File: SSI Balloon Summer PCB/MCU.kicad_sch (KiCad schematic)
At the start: 19 parts, among them J5 Conn_01x05, J9 Camera, SW2 SW_SPST, SW3 SW_SPST, U7 STM32F411CEUx, Y1 ABM8W-12.0000MHZ-8-K1Z-T3

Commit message: fixed TX and RX
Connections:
- net APRS_RX: now also U7.12 (PA2); no longer U7.13 (PA3)
- net APRS_TX: now also U7.13 (PA3); no longer U7.12 (PA2)
- net GPS_RX: now also U7.30 (PA9); no longer U7.31 (PA10)
- net GPS_TX: now also U7.31 (PA10); no longer U7.30 (PA9)
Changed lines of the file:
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@@
 		)
 	)
-	(label "GPS_TX"
+	(label "GPS_RX"
 		(at 107.95 73.66 0)
 		(effects
@@
 		)
 	)
-	(label "APRS_TX"
+	(label "APRS_RX"
 		(at 99.06 55.88 0)
 		(effects
@@
 		)
 	)
-	(label "APRS_RX"
+	(label "APRS_TX"
 		(at 107.95 58.42 0)
 		(effects
@@
 		)
 	)
-	(label "GPS_RX"
+	(label "GPS_TX"
 		(at 99.06 76.2 0)
 		(effects

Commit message: stuff
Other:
- note added: "Add pull up resistors for I2C Look at datasheet"
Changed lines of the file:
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@@
+		)
+	)
+	(text "Add pull up resistors for I2C\nLook at datasheet\n"
+		(exclude_from_sim no)
+		(at 107.95 98.552 0)
+		(effects
+			(font
+				(size 1.27 1.27)
+			)
 		)
 	)

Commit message: Fixed I2C and SPI issues
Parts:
- added R27: 10k, symbol Device:R
- added R28, R29: 4.7k, symbol Device:R
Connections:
- net +3V3: now also R28.2, R29.2
- net +5V: now also R27.2
- net Cam_CS: now also R27.1
- net SCL: now also R28.1
- net SDA: now also R29.1
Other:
- note added: "APRS_AUDIO DON"T FORGET"
- note removed: "Add pull up resistors for I2C Look at datasheet"

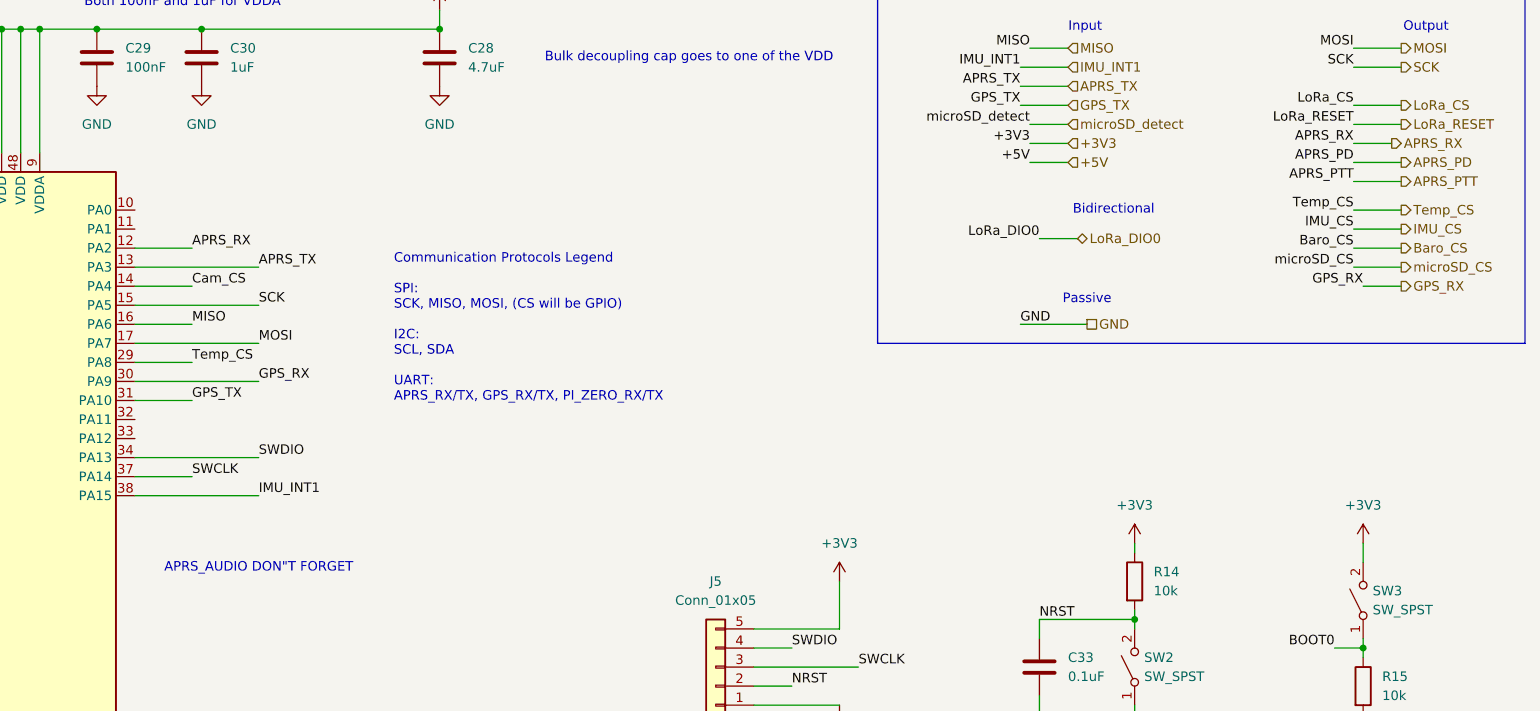
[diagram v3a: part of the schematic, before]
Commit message: Added APRS_AUDIO
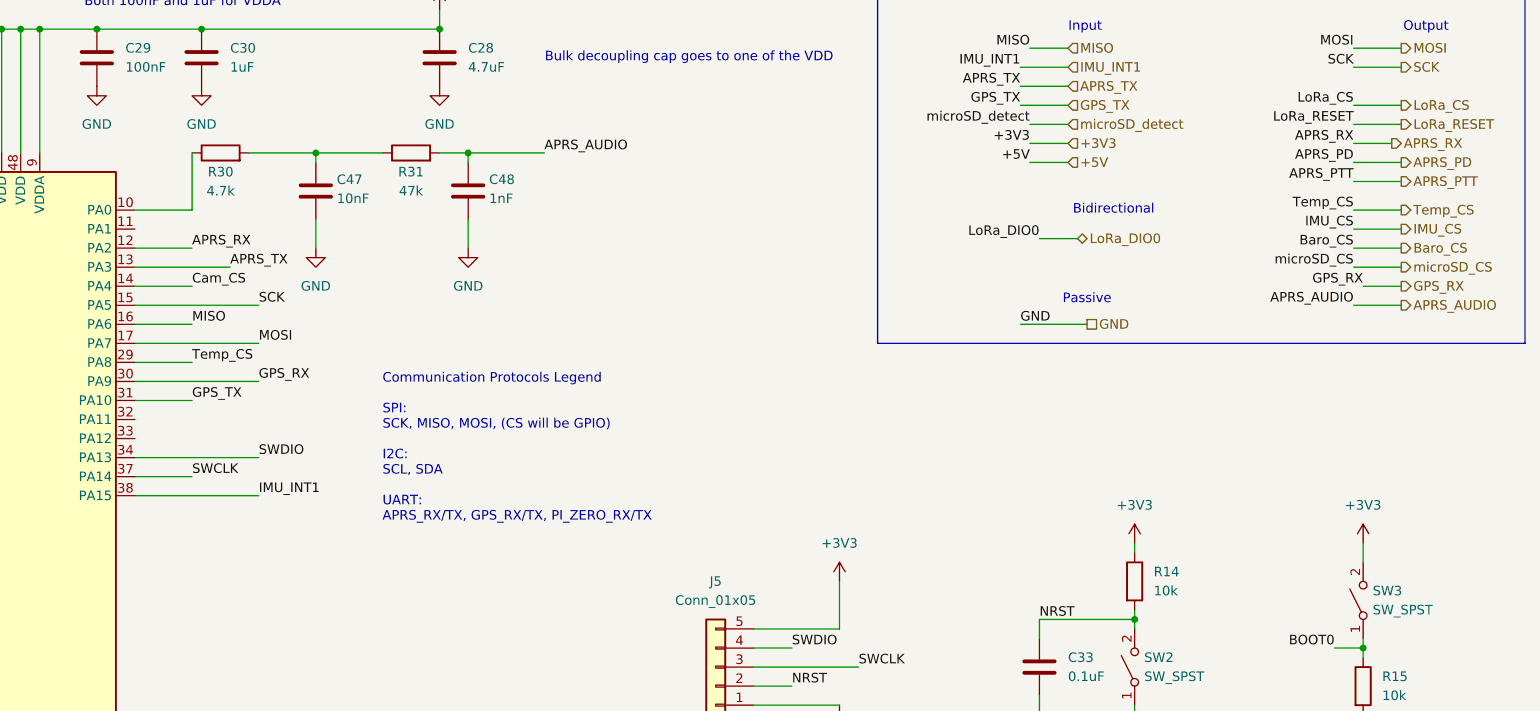
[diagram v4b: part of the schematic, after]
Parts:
- added C47: 10nF, symbol Device:C
- added C48: 1nF, symbol Device:C
- added R30: 4.7k, symbol Device:R
- added R31: 47k, symbol Device:R
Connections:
- net GND: now also C47.2, C48.2
- net at U7.10 (PA0): now also R30.1
- new net: C47.1, R30.2, R31.1
- new net APRS_AUDIO: C48.1, R31.2
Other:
- note removed: "APRS_AUDIO DON"T FORGET"

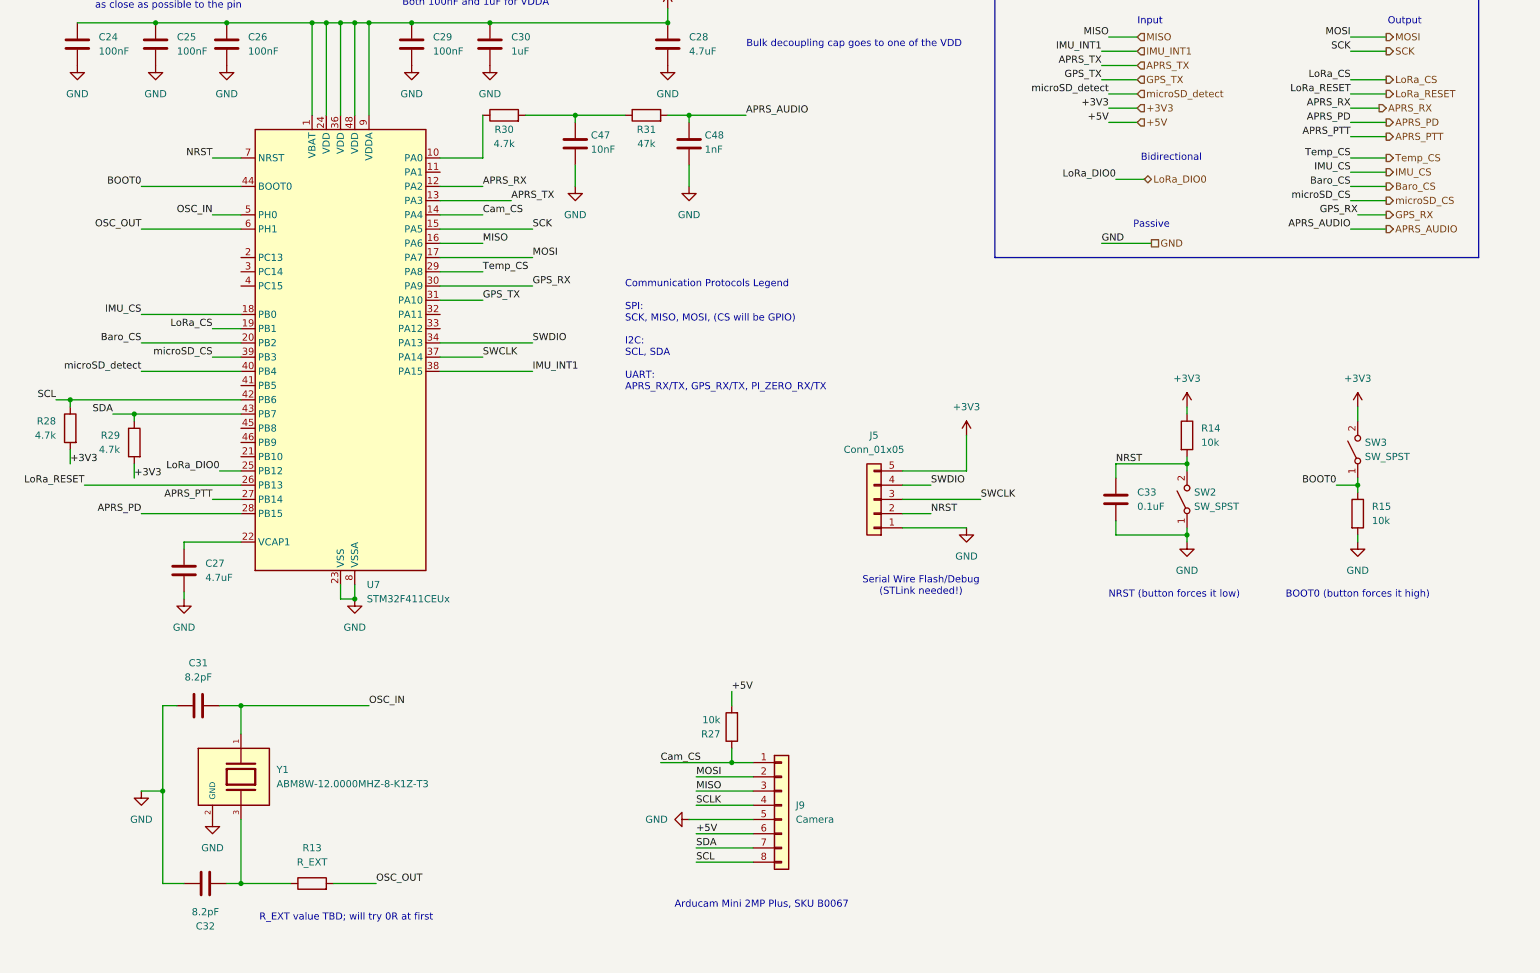
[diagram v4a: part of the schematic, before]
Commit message: Minor tweaks, renamed some pins
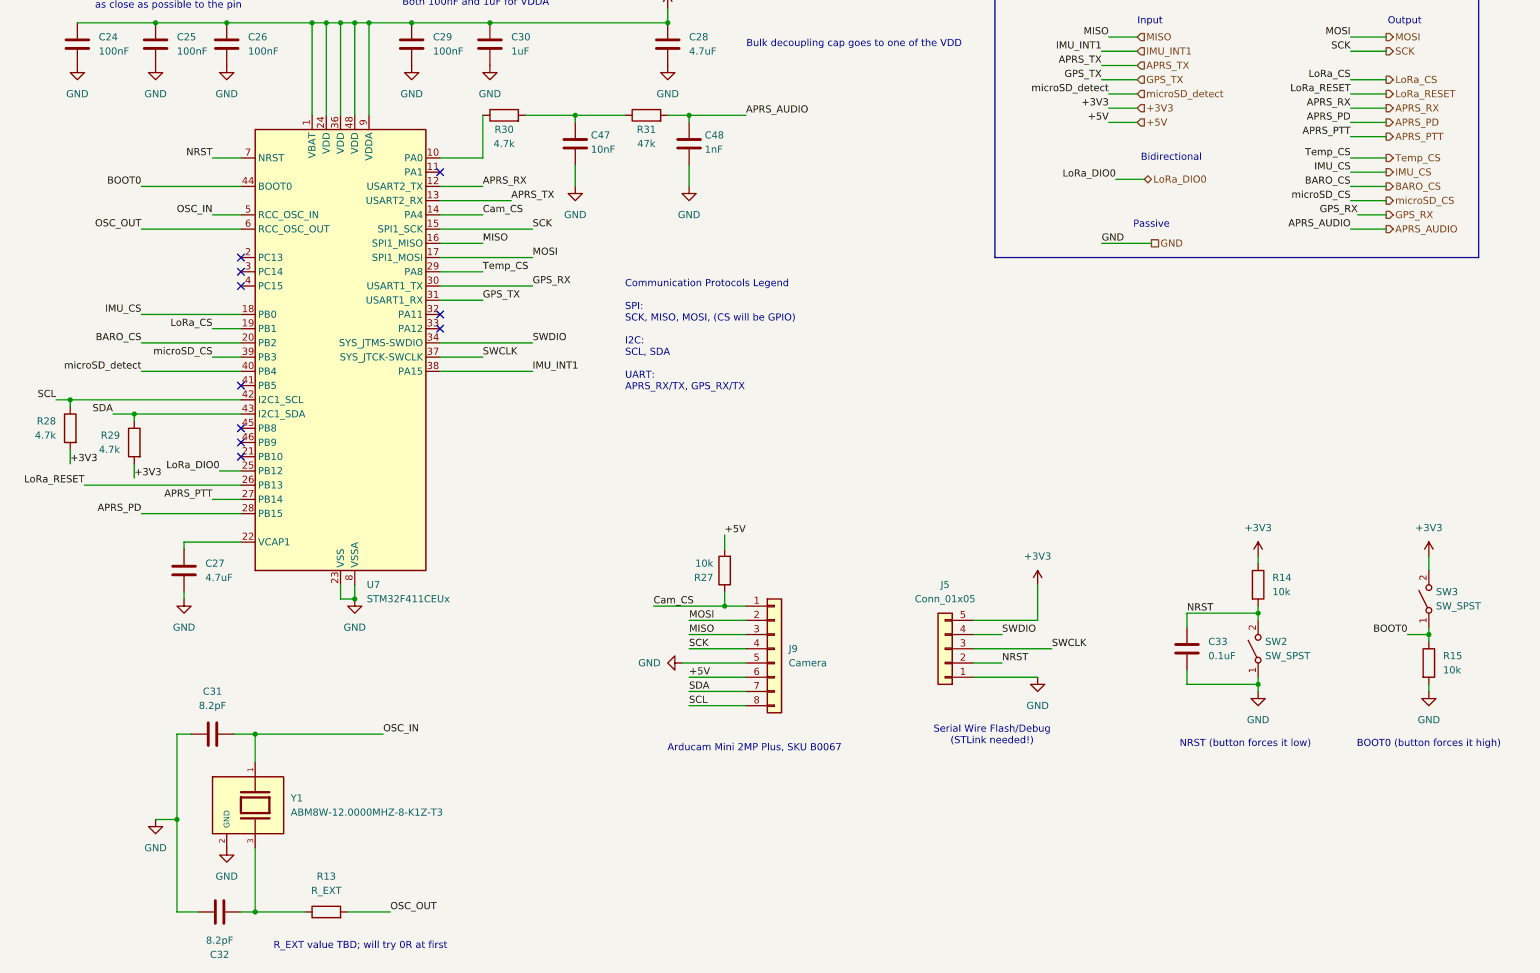
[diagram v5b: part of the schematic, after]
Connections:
- net SCLK is gone; now on net SCK: J9.4 (Pin_4)
- net Baro_CS renamed BARO_CS
- no-connect marks 0 -> 10
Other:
- note added: "Communication Protocols Legend SPI: SCK, MISO, MOSI, (CS will be GPIO) I2C: SCL, SDA UART: APRS_RX/TX, GPS_RX/TX"
- note removed: "Communication Protocols Legend SPI: SCK, MISO, MOSI, (CS will be GPIO) I2C: SCL, SDA UART: APRS_RX/TX, GPS_RX/TX, PI_ZERO_RX/TX"
- moved on the sheet: C31, C32, C33, J5, J9, R13, R14, R15, R27, SW2, SW3, Y1

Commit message: Layout placement for every sheet except PWR and SD card
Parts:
- added C49: 100nF, Capacitor_SMD:C_0603_1608Metric, symbol Device:C
- C24, C25, C26, C29, C30, C31, C32, C33, C47, C48: footprint (none) -> Capacitor_SMD:C_0603_1608Metric
- C27, C28: footprint (none) -> Capacitor_SMD:C_0805_2012Metric
- J9: footprint (none) -> Connector_PinHeader_2.54mm:PinHeader_1x08_P2.54mm_Vertical
- R13, R14, R15, R27, R28, R29, R30, R31: footprint (none) -> Resistor_SMD:R_0603_1608Metric
- SW2, SW3: footprint (none) -> Button_Switch_SMD:SW_Push_1P1T-MP_NO_Horizontal_Alps_SKRTLAE010
- Y1: footprint ABM8W-12.0000MHZ-8-K1Z-T3:XTAL_ABM8W-12.0000MHZ-8-K1Z-T3 -> Crystal:Crystal_SMD_3225-4Pin_3.2x2.5mm
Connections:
- net +3V3: now also C49.1
- net GND: now also C49.2
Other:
- note added: "NEED TO DETERMINE WHAT BUTTON FOR A MORE ACCURATE FOOTPRINT"
- moved on the sheet: C30

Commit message: Reviewed sensor sheet
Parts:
- removed C49: 100nF, Capacitor_SMD:C_0603_1608Metric, symbol Device:C
- C24, C25, C26, C29, C30, C31, C32, C33, C47, C48: footprint Capacitor_SMD:C_0603_1608Metric -> (none)
- C27, C28: footprint Capacitor_SMD:C_0805_2012Metric -> (none)
- J9: footprint Connector_PinHeader_2.54mm:PinHeader_1x08_P2.54mm_Vertical -> (none)
- R13, R14, R15, R27, R28, R29, R30, R31: footprint Resistor_SMD:R_0603_1608Metric -> (none)
- SW2, SW3: footprint Button_Switch_SMD:SW_Push_1P1T-MP_NO_Horizontal_Alps_SKRTLAE010 -> (none)
- Y1: footprint Crystal:Crystal_SMD_3225-4Pin_3.2x2.5mm -> ABM8W-12.0000MHZ-8-K1Z-T3:XTAL_ABM8W-12.0000MHZ-8-K1Z-T3
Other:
- note removed: "NEED TO DETERMINE WHAT BUTTON FOR A MORE ACCURATE FOOTPRINT"
- moved on the sheet: C30

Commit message: Overhauled power symbols for consistency and ERC
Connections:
- net +3V3: now also R28.1, R29.1; no longer R28.2, R29.2
- net SCL: now also R28.2; no longer R28.1
- net SDA: now also R29.2; no longer R29.1
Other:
- note removed: "Passive"
- moved on the sheet: C24, C25, C26, C27, C28, C29, C30, C31, C32, C33, C47, C48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
